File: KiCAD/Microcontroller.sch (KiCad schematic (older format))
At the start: 174 parts, among them J4 0.1\" HDR, SW1 JS202011SCQN, SW2 EVQ-Q2B03W, U2 STM32H743ZITx, U3 USB3300-EZK, Y1 24MHz, Y2 24MHz

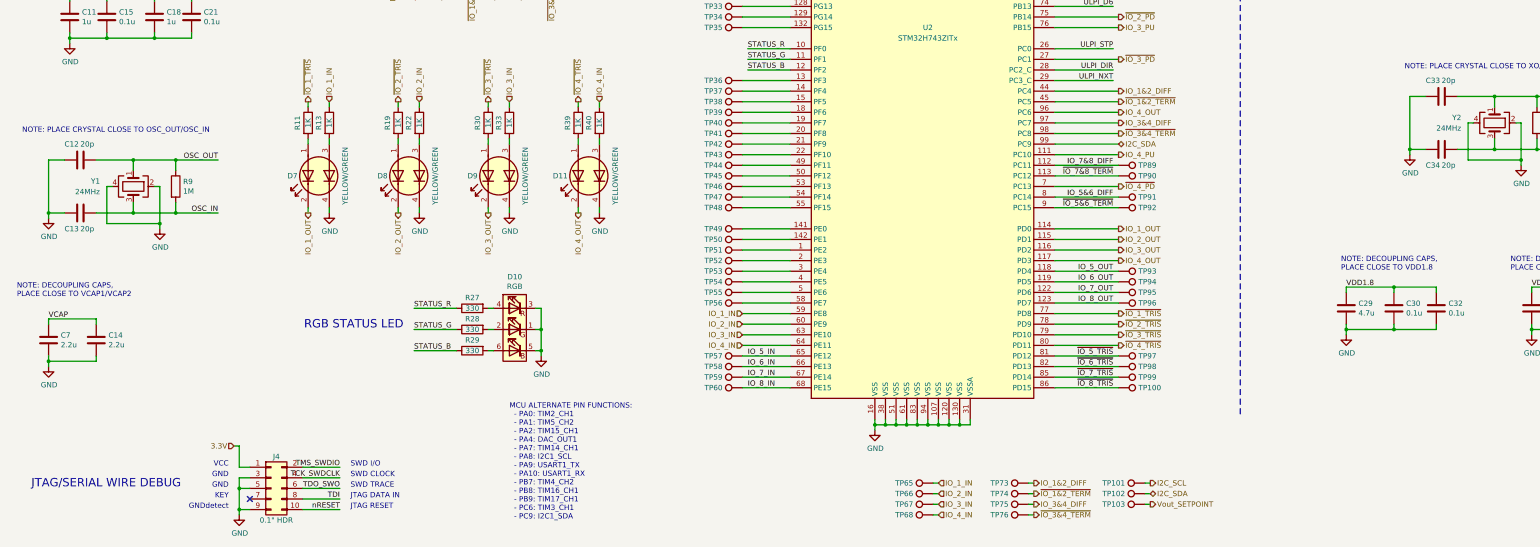
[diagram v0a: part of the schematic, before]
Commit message: Add power changeover circuit, fix minor issues
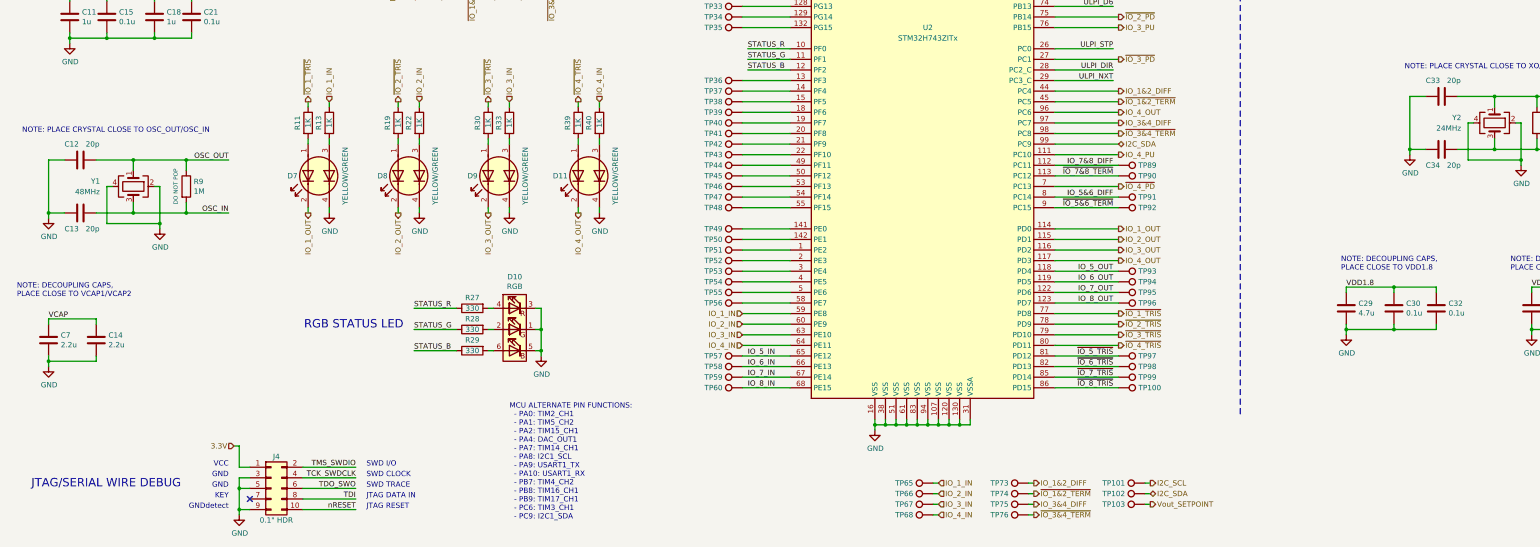
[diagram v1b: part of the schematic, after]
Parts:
- R9: Depop (none) -> DO NOT POP
- Y1: value 24MHz -> 48MHz
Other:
- moved on the sheet: R9
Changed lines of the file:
@@
 Sheet 2 10
 Title "MICROCONTROLLER SUBSYSTEM"
-Date "2020-02-03"
+Date "2020-02-04"
 Rev "A"
 Comp "THE UNIVERSITY OF AKRON"
@@
 P 14200 6250
 F 0 "C33" V 14350 6100 50  0000 L CNN
-F 1 "20p" V 14350 6250 50  0000 L CNN
+F 1 "20p" V 14350 6300 50  0000 L CNN
 F 2 "" H 14238 6100 50  0001 C CNN
 F 3 "~" H 14200 6250 50  0001 C CNN
@@
 	0    1    -1   0
 $EndComp
-Text Label 3800 9850 2    50   ~ 0
+Text Label 3950 9850 2    50   ~ 0
 TCK_SWDCLK
-Text Label 3800 9750 2    50   ~ 0
+Text Label 3950 9750 2    50   ~ 0
 TMS_SWDIO
-Text Label 3800 9950 2    50   ~ 0
+Text Label 3950 9950 2    50   ~ 0
 TDO_SWO
-Text Label 3800 10050 2    50   ~ 0
+Text Label 3950 10050 2    50   ~ 0
 TDI
-Text Label 3800 10150 2    50   ~ 0
+Text Label 3950 10150 2    50   ~ 0
 nRESET
 Text Label 11100 4500 2    50   ~ 0
@@
 P 14200 6750
 F 0 "C34" V 14350 6600 50  0000 L CNN
-F 1 "20p" V 14350 6750 50  0000 L CNN
+F 1 "20p" V 14350 6800 50  0000 L CNN
 F 2 "" H 14238 6600 50  0001 C CNN
 F 3 "~" H 14200 6750 50  0001 C CNN
@@
 	11100 3700 10550 3700
 Wire Wire Line
-	3800 9750 3450 9750
-Wire Wire Line
-	3800 9850 3450 9850
+	3950 9750 3450 9750
+Wire Wire Line
+	3950 9850 3450 9850
 Wire Wire Line
 	11100 3800 10550 3800
-Text Notes 3900 9750 0    50   ~ 0
+Text Notes 4050 9750 0    50   ~ 0
 SWD I/O
-Text Notes 3900 9850 0    50   ~ 0
+Text Notes 4050 9850 0    50   ~ 0
 SWD CLOCK
 Wire Wire Line
-	3800 9950 3450 9950
-Text Notes 3900 9950 0    50   ~ 0
+	3950 9950 3450 9950
+Text Notes 4050 9950 0    50   ~ 0
 SWD TRACE
 Wire Wire Line
 	11100 4400 10550 4400
-Text Notes 3900 10050 0    50   ~ 0
+Text Notes 4050 10050 0    50   ~ 0
 JTAG DATA IN
 Wire Wire Line
-	3800 10050 3450 10050
+	3950 10050 3450 10050
 Text Label 11100 3900 2    50   ~ 0
 TDI
@@
 	10550 3900 11100 3900
 Wire Wire Line
-	3800 10150 3450 10150
-Text Notes 3900 10150 0    50   ~ 0
+	3950 10150 3450 10150
+Text Notes 4050 10150 0    50   ~ 0
 JTAG RESET
 Wire Wire Line
@@
 NOTE: PLACE CRYSTAL CLOSE TO OSC_OUT/OSC_IN
 Wire Wire Line
-	2250 7350 2650 7350
-Text Label 2650 7350 2    50   ~ 0
+	2350 7350 2750 7350
+Text Label 2750 7350 2    50   ~ 0
 OSC_IN
-Text Label 2650 6850 2    50   ~ 0
+Text Label 2750 6850 2    50   ~ 0
 OSC_OUT
 $Comp
@@
 P 1350 7350
 F 0 "C13" V 1500 7200 50  0000 L CNN
-F 1 "20p" V 1500 7350 50  0000 L CNN
+F 1 "20p" V 1500 7400 50  0000 L CNN
 F 2 "" H 1388 7200 50  0001 C CNN
 F 3 "~" H 1350 7350 50  0001 C CNN
@@
 L Device:R R9
 U 1 1 607F1C2F
-P 2250 7100
-F 0 "R9" H 2320 7146 50  0000 L CNN
-F 1 "1M" H 2320 7055 50  0000 L CNN
-F 2 "" V 2180 7100 50  0001 C CNN
-F 3 "~" H 2250 7100 50  0001 C CNN
-	1    2250 7100
-	1    0    0    -1
-$EndComp
-Wire Wire Line
-	2650 6850 2250 6850
+P 2350 7100
+F 0 "R9" H 2420 7146 50  0000 L CNN
+F 1 "1M" H 2420 7055 50  0000 L CNN
+F 2 "" V 2280 7100 50  0001 C CNN
+F 3 "~" H 2350 7100 50  0001 C CNN
+F 4 "DO NOT POP" V 2250 7100 39  0000 C CNN "Depop"
+	1    2350 7100
+	1    0    0    -1
+$EndComp
+Wire Wire Line
+	2750 6850 2350 6850
 Wire Wire Line
 	1200 6850 1050 6850
@@
 	1650 7100 1600 7100
 Wire Wire Line
-	2250 6850 1850 6850
+	2350 6850 1850 6850
 Wire Wire Line
 	1850 6850 1850 6950
 Wire Wire Line
-	2250 7350 1850 7350
+	2350 7350 1850 7350
 Wire Wire Line
 	1850 7250 1850 7350
-Connection ~ 2250 7350
-Connection ~ 2250 6850
+Connection ~ 2350 7350
+Connection ~ 2350 6850
 $Comp
 L Device:Crystal_GND24 Y1
@@
 P 1850 7100
 F 0 "Y1" V 1800 6700 50  0000 L CNN
-F 1 "24MHz" V 1900 6550 50  0000 L CNN
+F 1 "48MHz" V 1900 6550 50  0000 L CNN
 F 2 "" H 1850 7100 50  0001 C CNN
 F 3 "~" H 1850 7100 50  0001 C CNN
@@
 P 1350 6850
 F 0 "C12" V 1500 6700 50  0000 L CNN
-F 1 "20p" V 1500 6850 50  0000 L CNN
+F 1 "20p" V 1500 6900 50  0000 L CNN
 F 2 "" H 1388 6700 50  0001 C CNN
 F 3 "~" H 1350 6850 50  0001 C CNN
@@
 $EndComp
 Wire Wire Line
-	2250 6950 2250 6850
-Wire Wire Line
-	2250 7350 2250 7250
+	2350 6950 2350 6850
+Wire Wire Line
+	2350 7350 2350 7250
 Text Label 7650 3800 0    50   ~ 0
 OSC_OUT

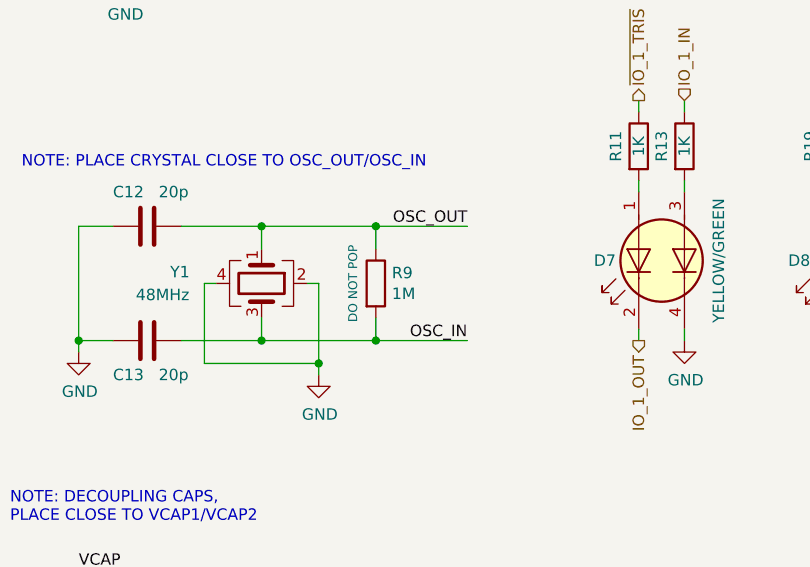
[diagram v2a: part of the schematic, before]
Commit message: Assign footprints, fix minor schematic issues
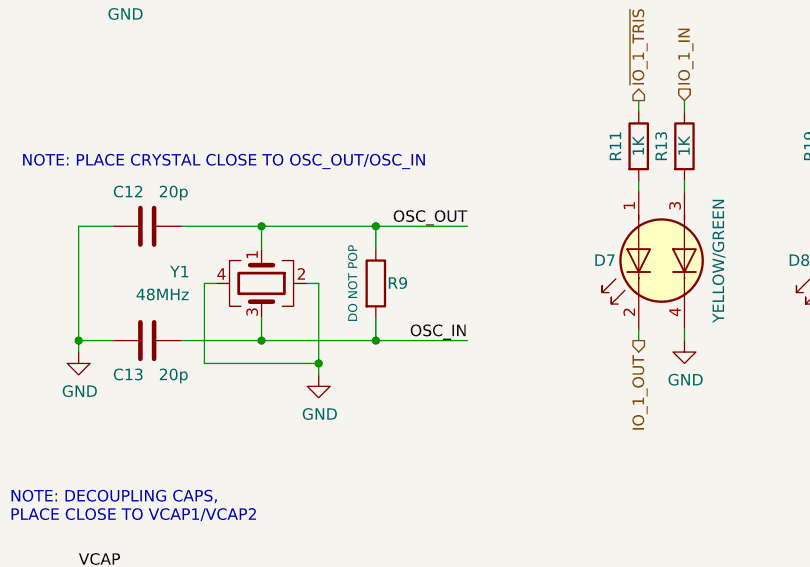
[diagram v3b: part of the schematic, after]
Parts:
- C10, C11, C12, C13, C15, C16, C17, C18, C19, C20, C21, C22, C23, C24, C25, C26, C27, C28, C30, C31, C32, C33, C34, C35, C36, C38, C39, C9: footprint (none) -> Capacitor_SMD:C_0603_1608Metric
- C14, C29, C37, C7, C8: footprint (none) -> Capacitor_SMD:C_0805_2012Metric
- D10: footprint (none) -> io-master:LED_Everlight_19-337C
- D11, D7, D8, D9: footprint (none) -> io-master:LED_Kingbright_APTB1615YSGC
- D12: footprint (none) -> Diode_SMD:D_SOD-323F
- FB1, R10, R11, R12, R13, R14, R15, R16, R17, R18, R19, R20, R21, R22, R23, R24, R25, R26, R27, R28, R29, R30, R31, R32, R33, R34, R35, R36, R37, R38, R39, R40, R41, R42, R43, R44, R45, R46: footprint (none) -> Resistor_SMD:R_0603_1608Metric
- J4: footprint (none) -> Connector_PinSocket_2.54mm:PinSocket_2x05_P2.54mm_Vertical
- R9: value 1M -> R; footprint (none) -> Resistor_SMD:R_0603_1608Metric
- SW1: footprint (none) -> io-master:SW_DPDT_CK_JS202011SCQN
- SW2: footprint (none) -> Button_Switch_SMD:SW_SPST_EVQQ2
- TP100: value TestPoint -> TRIS8; footprint (none) -> TestPoint:TestPoint_Pad_D1.0mm
- TP101: value TestPoint -> SCL; footprint (none) -> TestPoint:TestPoint_Pad_D1.0mm
- TP102: value TestPoint -> SDA; footprint (none) -> TestPoint:TestPoint_Pad_D1.0mm
- TP103: value TestPoint -> VSET; footprint (none) -> TestPoint:TestPoint_Pad_D1.0mm
- TP104: value TestPoint -> PD1; footprint (none) -> TestPoint:TestPoint_Pad_D1.0mm
- TP105: value TestPoint -> PD2; footprint (none) -> TestPoint:TestPoint_Pad_D1.0mm
- TP106: value TestPoint -> PD3; footprint (none) -> TestPoint:TestPoint_Pad_D1.0mm
- TP107: value TestPoint -> PD4; footprint (none) -> TestPoint:TestPoint_Pad_D1.0mm
- TP174: value TestPoint -> PRST; footprint (none) -> TestPoint:TestPoint_Pad_D1.0mm
- TP20: value TestPoint -> PU5; footprint (none) -> TestPoint:TestPoint_Pad_D1.0mm
- TP21: value TestPoint -> PD5; footprint (none) -> TestPoint:TestPoint_Pad_D1.0mm
- TP22: value TestPoint -> PU6; footprint (none) -> TestPoint:TestPoint_Pad_D1.0mm
- TP23: value TestPoint -> PD6; footprint (none) -> TestPoint:TestPoint_Pad_D1.0mm
- TP24: value TestPoint -> PU7; footprint (none) -> TestPoint:TestPoint_Pad_D1.0mm
- TP25: value TestPoint -> PD7; footprint (none) -> TestPoint:TestPoint_Pad_D1.0mm
- TP26: value TestPoint -> PU8; footprint (none) -> TestPoint:TestPoint_Pad_D1.0mm
- TP27: value TestPoint -> PD8; footprint (none) -> TestPoint:TestPoint_Pad_D1.0mm
- TP28: value TestPoint -> PG8; footprint (none) -> TestPoint:TestPoint_Pad_D1.0mm
- TP29: value TestPoint -> PG9; footprint (none) -> TestPoint:TestPoint_Pad_D1.0mm
- TP30: value TestPoint -> PG10; footprint (none) -> TestPoint:TestPoint_Pad_D1.0mm
- TP31: value TestPoint -> PG11; footprint (none) -> TestPoint:TestPoint_Pad_D1.0mm
- TP32: value TestPoint -> PG12; footprint (none) -> TestPoint:TestPoint_Pad_D1.0mm
- TP33: value TestPoint -> PG13; footprint (none) -> TestPoint:TestPoint_Pad_D1.0mm
- TP34: value TestPoint -> PG14; footprint (none) -> TestPoint:TestPoint_Pad_D1.0mm
- TP35: value TestPoint -> PG15; footprint (none) -> TestPoint:TestPoint_Pad_D1.0mm
- TP36: value TestPoint -> PF3; footprint (none) -> TestPoint:TestPoint_Pad_D1.0mm
- TP37: value TestPoint -> PF4; footprint (none) -> TestPoint:TestPoint_Pad_D1.0mm
- TP38: value TestPoint -> PF5; footprint (none) -> TestPoint:TestPoint_Pad_D1.0mm
- TP39: value TestPoint -> PF6; footprint (none) -> TestPoint:TestPoint_Pad_D1.0mm
- TP40: value TestPoint -> PF7; footprint (none) -> TestPoint:TestPoint_Pad_D1.0mm
- TP41: value TestPoint -> PF8; footprint (none) -> TestPoint:TestPoint_Pad_D1.0mm
- TP42: value TestPoint -> PF9; footprint (none) -> TestPoint:TestPoint_Pad_D1.0mm
- TP43: value TestPoint -> PF10; footprint (none) -> TestPoint:TestPoint_Pad_D1.0mm
- TP44: value TestPoint -> PF11; footprint (none) -> TestPoint:TestPoint_Pad_D1.0mm
- TP45: value TestPoint -> PF12; footprint (none) -> TestPoint:TestPoint_Pad_D1.0mm
- TP46: value TestPoint -> PF13; footprint (none) -> TestPoint:TestPoint_Pad_D1.0mm
- TP47: value TestPoint -> PF14; footprint (none) -> TestPoint:TestPoint_Pad_D1.0mm
- TP48: value TestPoint -> PF15; footprint (none) -> TestPoint:TestPoint_Pad_D1.0mm
- TP49: value TestPoint -> PE0; footprint (none) -> TestPoint:TestPoint_Pad_D1.0mm
- TP50: value TestPoint -> PE1; footprint (none) -> TestPoint:TestPoint_Pad_D1.0mm
- TP51: value TestPoint -> PE2; footprint (none) -> TestPoint:TestPoint_Pad_D1.0mm
- TP52: value TestPoint -> PE3; footprint (none) -> TestPoint:TestPoint_Pad_D1.0mm
- TP53: value TestPoint -> PE4; footprint (none) -> TestPoint:TestPoint_Pad_D1.0mm
- TP54: value TestPoint -> PE5; footprint (none) -> TestPoint:TestPoint_Pad_D1.0mm
- TP55: value TestPoint -> PE6; footprint (none) -> TestPoint:TestPoint_Pad_D1.0mm
- TP56: value TestPoint -> PE7; footprint (none) -> TestPoint:TestPoint_Pad_D1.0mm
- TP57: value TestPoint -> PE12; footprint (none) -> TestPoint:TestPoint_Pad_D1.0mm
- TP58: value TestPoint -> PE13; footprint (none) -> TestPoint:TestPoint_Pad_D1.0mm
- TP59: value TestPoint -> PE14; footprint (none) -> TestPoint:TestPoint_Pad_D1.0mm
- TP60: value TestPoint -> PE15; footprint (none) -> TestPoint:TestPoint_Pad_D1.0mm
- TP61: value TestPoint -> OUT1; footprint (none) -> TestPoint:TestPoint_Pad_D1.0mm
- TP62: value TestPoint -> OUT2; footprint (none) -> TestPoint:TestPoint_Pad_D1.0mm
- TP63: value TestPoint -> OUT3; footprint (none) -> TestPoint:TestPoint_Pad_D1.0mm
- TP64: value TestPoint -> OUT4; footprint (none) -> TestPoint:TestPoint_Pad_D1.0mm
- TP65: value TestPoint -> IN1; footprint (none) -> TestPoint:TestPoint_Pad_D1.0mm
- TP66: value TestPoint -> IN2; footprint (none) -> TestPoint:TestPoint_Pad_D1.0mm
- TP67: value TestPoint -> IN3; footprint (none) -> TestPoint:TestPoint_Pad_D1.0mm
- TP68: value TestPoint -> IN4; footprint (none) -> TestPoint:TestPoint_Pad_D1.0mm
- TP69: value TestPoint -> TRIS1; footprint (none) -> TestPoint:TestPoint_Pad_D1.0mm
- TP70: value TestPoint -> TRIS2; footprint (none) -> TestPoint:TestPoint_Pad_D1.0mm
- TP71: value TestPoint -> TRIS3; footprint (none) -> TestPoint:TestPoint_Pad_D1.0mm
- TP72: value TestPoint -> TRIS4; footprint (none) -> TestPoint:TestPoint_Pad_D1.0mm
- TP73: value TestPoint -> DIFF12; footprint (none) -> TestPoint:TestPoint_Pad_D1.0mm
- TP74: value TestPoint -> TERM12; footprint (none) -> TestPoint:TestPoint_Pad_D1.0mm
- TP75: value TestPoint -> DIFF34; footprint (none) -> TestPoint:TestPoint_Pad_D1.0mm
- TP76: value TestPoint -> TERM34; footprint (none) -> TestPoint:TestPoint_Pad_D1.0mm
- TP77: value TestPoint -> PU1; footprint (none) -> TestPoint:TestPoint_Pad_D1.0mm
- TP78: value TestPoint -> PU2; footprint (none) -> TestPoint:TestPoint_Pad_D1.0mm
- TP79: value TestPoint -> PU3; footprint (none) -> TestPoint:TestPoint_Pad_D1.0mm
- TP80: value TestPoint -> PU4; footprint (none) -> TestPoint:TestPoint_Pad_D1.0mm
- TP81, TP96: value TestPoint -> OUT8; footprint (none) -> TestPoint:TestPoint_Pad_D1.0mm
- TP82: value TestPoint -> TXO; footprint (none) -> TestPoint:TestPoint_Pad_D1.0mm
- TP83: value TestPoint -> RXI; footprint (none) -> TestPoint:TestPoint_Pad_D1.0mm
- TP84: value TestPoint -> DM; footprint (none) -> TestPoint:TestPoint_Pad_D1.0mm
- TP85: value TestPoint -> DP; footprint (none) -> TestPoint:TestPoint_Pad_D1.0mm
- TP86, TP93: value TestPoint -> OUT5; footprint (none) -> TestPoint:TestPoint_Pad_D1.0mm
- TP87, TP94: value TestPoint -> OUT6; footprint (none) -> TestPoint:TestPoint_Pad_D1.0mm
- TP88, TP95: value TestPoint -> OUT7; footprint (none) -> TestPoint:TestPoint_Pad_D1.0mm
- TP89: value TestPoint -> DIFF78; footprint (none) -> TestPoint:TestPoint_Pad_D1.0mm
- TP90: value TestPoint -> TERM78; footprint (none) -> TestPoint:TestPoint_Pad_D1.0mm
- TP91: value TestPoint -> DIFF56; footprint (none) -> TestPoint:TestPoint_Pad_D1.0mm
- TP92: value TestPoint -> TERM56; footprint (none) -> TestPoint:TestPoint_Pad_D1.0mm
- TP97: value TestPoint -> TRIS5; footprint (none) -> TestPoint:TestPoint_Pad_D1.0mm
- TP98: value TestPoint -> TRIS6; footprint (none) -> TestPoint:TestPoint_Pad_D1.0mm
- TP99: value TestPoint -> TRIS7; footprint (none) -> TestPoint:TestPoint_Pad_D1.0mm
- Y1, Y2: footprint (none) -> io-master:Crystal_SMD_Murata_XRCGB

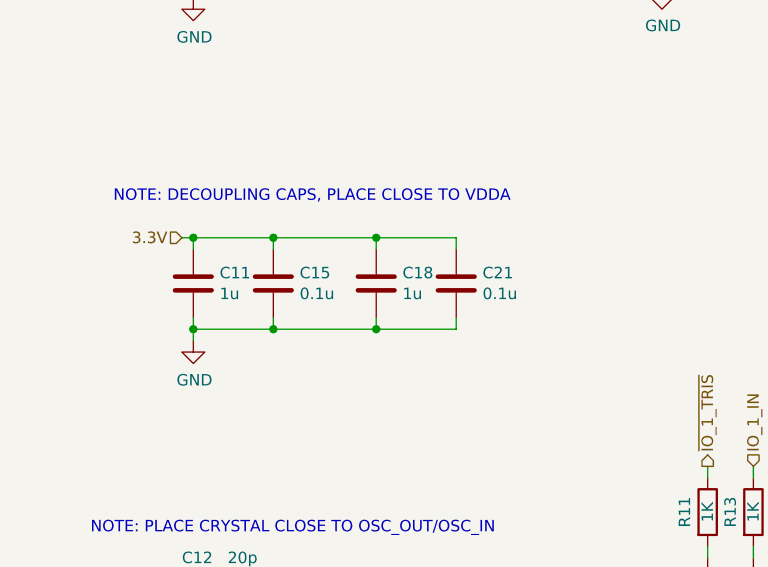
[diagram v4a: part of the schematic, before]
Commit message: Remove extra caps C18 and C21 on VDDA pin
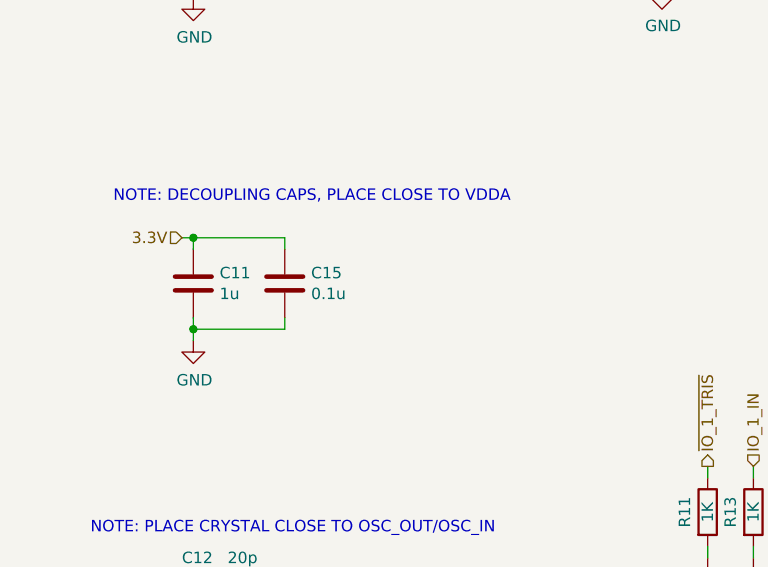
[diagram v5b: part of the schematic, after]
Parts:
- removed C18: 1u, Capacitor_SMD:C_0603_1608Metric, symbol Device:C
- removed C21: 0.1u, Capacitor_SMD:C_0603_1608Metric, symbol Device:C
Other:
- moved on the sheet: C15
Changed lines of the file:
@@
 L Device:C C15
 U 1 1 5E2E09A1
-P 1600 5500
-F 0 "C15" H 1715 5546 50  0000 L CNN
-F 1 "0.1u" H 1715 5455 50  0000 L CNN
-F 2 "Capacitor_SMD:C_0603_1608Metric" H 1638 5350 50  0001 C CNN
-F 3 "~" H 1600 5500 50  0001 C CNN
-	1    1600 5500
+P 1650 5500
+F 0 "C15" H 1765 5546 50  0000 L CNN
+F 1 "0.1u" H 1765 5455 50  0000 L CNN
+F 2 "Capacitor_SMD:C_0603_1608Metric" H 1688 5350 50  0001 C CNN
+F 3 "~" H 1650 5500 50  0001 C CNN
+	1    1650 5500
 	1    0    0    -1
 $EndComp
@@
 	1200 5300 1250 5300
 Wire Wire Line
-	1600 5300 1600 5350
+	1650 5300 1650 5350
 Wire Wire Line
 	1250 5350 1250 5300
 Connection ~ 1250 5300
 Wire Wire Line
-	1250 5300 1600 5300
+	1250 5300 1650 5300
 Wire Wire Line
 	1250 5750 1250 5700
 Wire Wire Line
-	1250 5700 1600 5700
-Wire Wire Line
-	1600 5700 1600 5650
+	1250 5700 1650 5700
+Wire Wire Line
+	1650 5700 1650 5650
 Connection ~ 1250 5700
 Wire Wire Line
@@
 BOOT SWITCH
 $Comp
-L Device:C C21
-U 1 1 5F9683A5
-P 2400 5500
-F 0 "C21" H 2515 5546 50  0000 L CNN
-F 1 "0.1u" H 2515 5455 50  0000 L CNN
-F 2 "Capacitor_SMD:C_0603_1608Metric" H 2438 5350 50  0001 C CNN
-F 3 "~" H 2400 5500 50  0001 C CNN
-	1    2400 5500
-	1    0    0    -1
-$EndComp
-$Comp
-L Device:C C18
-U 1 1 5F9683AF
-P 2050 5500
-F 0 "C18" H 2165 5546 50  0000 L CNN
-F 1 "1u" H 2165 5455 50  0000 L CNN
-F 2 "Capacitor_SMD:C_0603_1608Metric" H 2088 5350 50  0001 C CNN
-F 3 "~" H 2050 5500 50  0001 C CNN
-	1    2050 5500
-	1    0    0    -1
-$EndComp
-Wire Wire Line
-	1600 5300 2050 5300
-Wire Wire Line
-	2050 5300 2050 5350
-Connection ~ 1600 5300
-Wire Wire Line
-	2050 5300 2400 5300
-Wire Wire Line
-	2400 5300 2400 5350
-Connection ~ 2050 5300
-Wire Wire Line
-	1600 5700 2050 5700
-Wire Wire Line
-	2050 5700 2050 5650
-Connection ~ 1600 5700
-Wire Wire Line
-	2050 5700 2400 5700
-Wire Wire Line
-	2400 5700 2400 5650
-Connection ~ 2050 5700
-$Comp
 L MCU_ST_STM32H7:STM32H743ZITx U2
